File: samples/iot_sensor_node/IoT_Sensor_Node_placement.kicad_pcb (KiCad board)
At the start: 2 copper layers, 102 x 70 mm, 5 parts, among them J1 USB-C, U1 AP62300, U2 TLV75518, U3 ESP32-WROOM-32E, U4 BME280

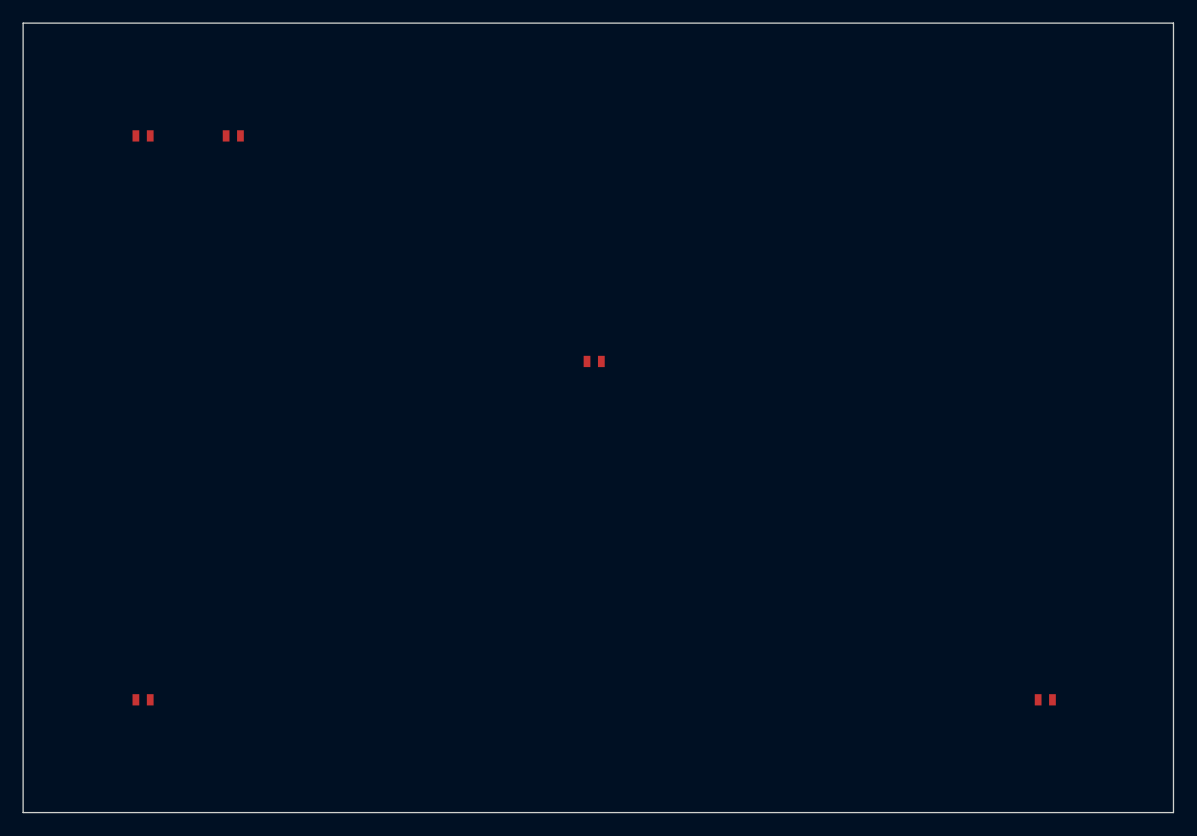
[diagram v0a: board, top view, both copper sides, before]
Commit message: chore: regenerate 8 sample designs against v0.27.0 engine
All 8 samples pass full validation (0 ERC errors):
- led_power_indicator, iot_sensor_node, usb_regulated_supply,
  usb_uart_bridge, oled_display_module, battery_iot_sensor,
  motor_controller, fpga_power_carrier

New artifacts per sample: .kicad_sch, _test_points.csv, _pinout.csv,
canonical_spec.yaml, design_ir.json, validation_report.json; MCU samples
also emit sdkconfig.defaults / .ioc stubs.

Also adds samples/*/svg/ to .gitignore — schematic SVG exports are
regenerable and too large to track.

zigbee_humidistat deferred: non-deterministic schematic output across
two generation runs (text annotation ordering vs sheet_instances).
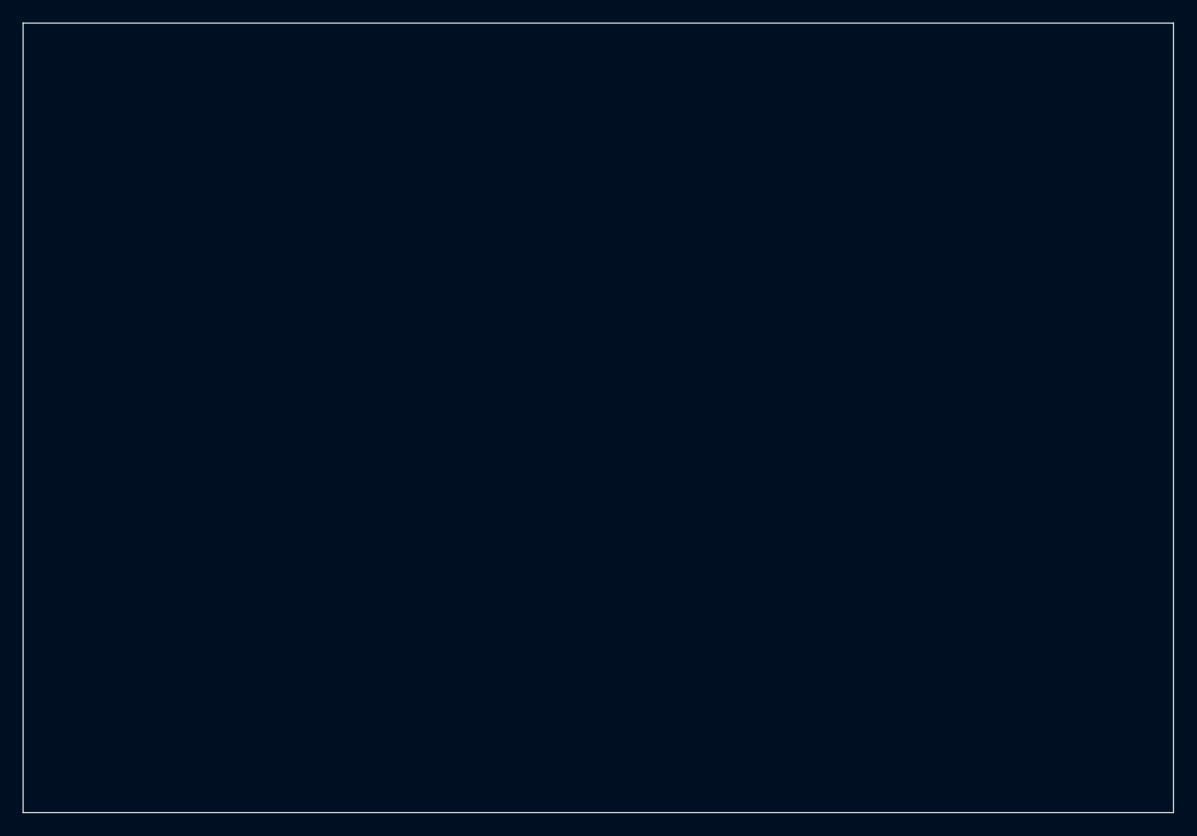
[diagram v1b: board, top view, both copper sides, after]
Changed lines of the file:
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@@
-(kicad_pcb (version 20240108) (generator "schematic_engine")
+(kicad_pcb (version 20240108) (generator "schematic_engine placement_preview")
   (general (thickness 1.6) (legacy_teardrops no))
   (layers
@@
       (effects (font (size 1.0 1.0) (thickness 0.15)))
     )
-    (pad "1" smd rect (at 0.00 0) (size 0.6 1.0) (layers "F.Cu" "F.Paste" "F.Mask") (net 14 "VBUS_5V"))
-    (pad "2" smd rect (at 1.27 0) (size 0.6 1.0) (layers "F.Cu" "F.Paste" "F.Mask") (net 6 "GND"))
   )
   (footprint "SOT-23-5"
@@
       (effects (font (size 1.0 1.0) (thickness 0.15)))
     )
-    (pad "1" smd rect (at 0.00 0) (size 0.6 1.0) (layers "F.Cu" "F.Paste" "F.Mask") (net 16 "VDD_3P3"))
-    (pad "2" smd rect (at 1.27 0) (size 0.6 1.0) (layers "F.Cu" "F.Paste" "F.Mask") (net 6 "GND"))
   )
   (footprint "RF_Module:ESP32-WROOM-32E"
@@
       (effects (font (size 1.0 1.0) (thickness 0.15)))
     )
-    (pad "1" smd rect (at 0.00 0) (size 0.6 1.0) (layers "F.Cu" "F.Paste" "F.Mask") (net 6 "GND"))
-    (pad "2" smd rect (at 1.27 0) (size 0.6 1.0) (layers "F.Cu" "F.Paste" "F.Mask") (net 16 "VDD_3P3"))
   )
   (footprint "Connector_USB:USB_C_Receptacle_GCT_USB4085"
@@
       (effects (font (size 1.0 1.0) (thickness 0.15)))
     )
-    (pad "1" smd rect (at 0.00 0) (size 0.6 1.0) (layers "F.Cu" "F.Paste" "F.Mask") (net 14 "VBUS_5V"))
-    (pad "2" smd rect (at 1.27 0) (size 0.6 1.0) (layers "F.Cu" "F.Paste" "F.Mask") (net 6 "GND"))
   )
   (footprint "Package_LGA:Bosch_LGA-8_2.5x2.5mm"
@@
       (effects (font (size 1.0 1.0) (thickness 0.15)))
     )
-    (pad "1" smd rect (at 0.00 0) (size 0.6 1.0) (layers "F.Cu" "F.Paste" "F.Mask") (net 6 "GND"))
-    (pad "2" smd rect (at 1.27 0) (size 0.6 1.0) (layers "F.Cu" "F.Paste" "F.Mask") (net 16 "VDD_3P3"))
   )
   (gr_line (start 0.00 0.00) (end 102.00 0.00) (stroke (width 0.1) (type solid)) (layer "Edge.Cuts"))
